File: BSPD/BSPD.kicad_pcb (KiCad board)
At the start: 2 copper layers, 81 x 61 mm, 32 parts, among them Q3 PMOS, U1 LM339DR, U10 641964-1, U2 SN74LVC1G08DBVR, U3 NE555DR, U4 SN74LVC3G14DCUR, U5 SN74AC32DR, U6 SN74LVC1G08DBVR, U7 641964-1, U8 R-78E5.0-0.5, U9 641964-1

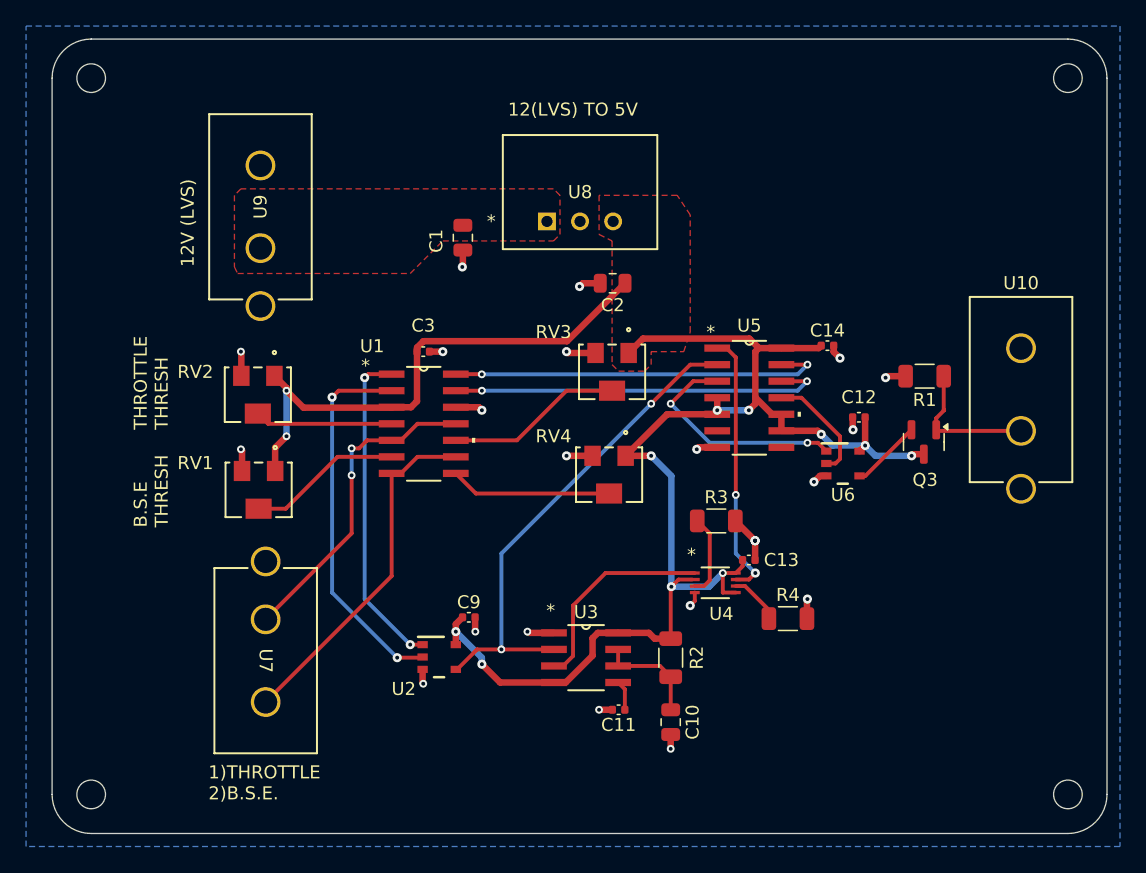
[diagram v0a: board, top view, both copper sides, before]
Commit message: Fixes to BSPD
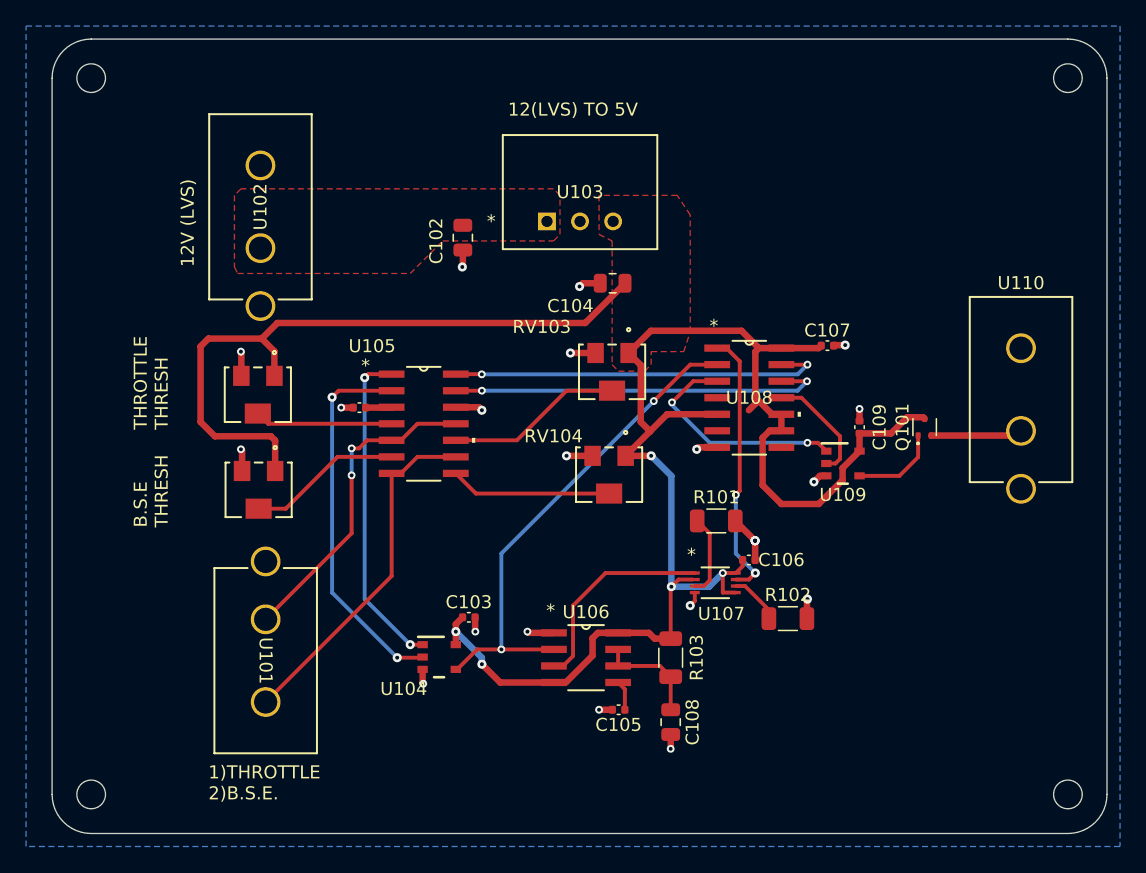
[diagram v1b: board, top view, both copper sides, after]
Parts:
- removed Q3: PMOS, Package_TO_SOT_SMD:SOT-23
- removed R1: 10K, Resistor_SMD:R_1206_3216Metric
- added Q101: Q_PMOS_GSD, Package_TO_SOT_SMD:SOT-523, F.Cu at (173.0, 116.8)
- U108: renamed from U5; footprint LM339DR:D14 -> SN74AC32DR:D14
- moved C101 6.52 mm to (129.6, 115.3), turned to 180 degrees
- moved C109 0.76 mm to (168.0, 116.8), turned to 90 degrees
- renumbered C3 to C101, C1 to C102, C9 to C103, C2 to C104, C11 to C105, C13 to C106, C14 to C107, C10 to C108, C12 to C109, H1 to H101, H2 to H102, H3 to H103, H4 to H104, R3 to R101, R4 to R102, R2 to R103, RV1 to RV101, RV2 to RV102, RV3 to RV103, RV4 to RV104, U7 to U101, U9 to U102, U8 to U103, U2 to U104, U1 to U105, U3 to U106, U4 to U107, U6 to U109, U10 to U110
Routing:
- net +5V: track 142.9 -> 167.8 mm, vias 12 -> 5
- net BSPD_TO_FAULT: track 10.9 -> 7.05 mm
- net GND: track 33.2 -> 30.8 mm, vias 22 -> 21
- net Net-(Q101-G): track 5.45 -> 6.75 mm
